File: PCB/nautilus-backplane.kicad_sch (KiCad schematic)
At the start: 85 parts

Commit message: Traced ethernet
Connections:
- removed net 0+: JP22.2 (B), JP40.3 (B), JP8.2 (B)
- removed net 0-: JP21.2 (B), JP40.2 (C), JP7.2 (B)
- net 0A+ renamed e2_0+
- net 0A- renamed e2_0-
- net 1+ renamed e1_1+
- net e1_1+: no longer JP20.2 (B)
- net 1- renamed e1_1-
- net e1_1-: no longer JP19.2 (B)
- net 1A+ renamed B12
- net B12: no longer JP24.2 (B)
- net 1A- renamed B13
- net B13: no longer JP23.2 (B)
- net 2+ renamed A19
- net A19: no longer JP4.2 (B)
- net 2- renamed A18
- net A18: no longer JP3.2 (B)
- net 3+ renamed A16
- net A16: no longer JP2.2 (B)
- net 3- renamed A17
- net A17: no longer JP1.2 (B)
- new net B18: JP40.2 (C)
- new net B19: JP40.3 (B)
- new net e1_0+: JP8.2 (B)
- new net e1_0-: JP7.2 (B)
- new net e1_2+: JP4.2 (B)
- new net e1_2-: JP3.2 (B)
- new net e1_3+: JP2.2 (B)
- new net e1_3-: JP1.2 (B)
- new net e2_1+: JP24.2 (B)
- new net e2_1-: JP23.2 (B)
- new net e2_2+: JP22.2 (B)
- new net e2_2-: JP21.2 (B)
- new net e2_3+: JP20.2 (B)
- new net e2_3-: JP19.2 (B)

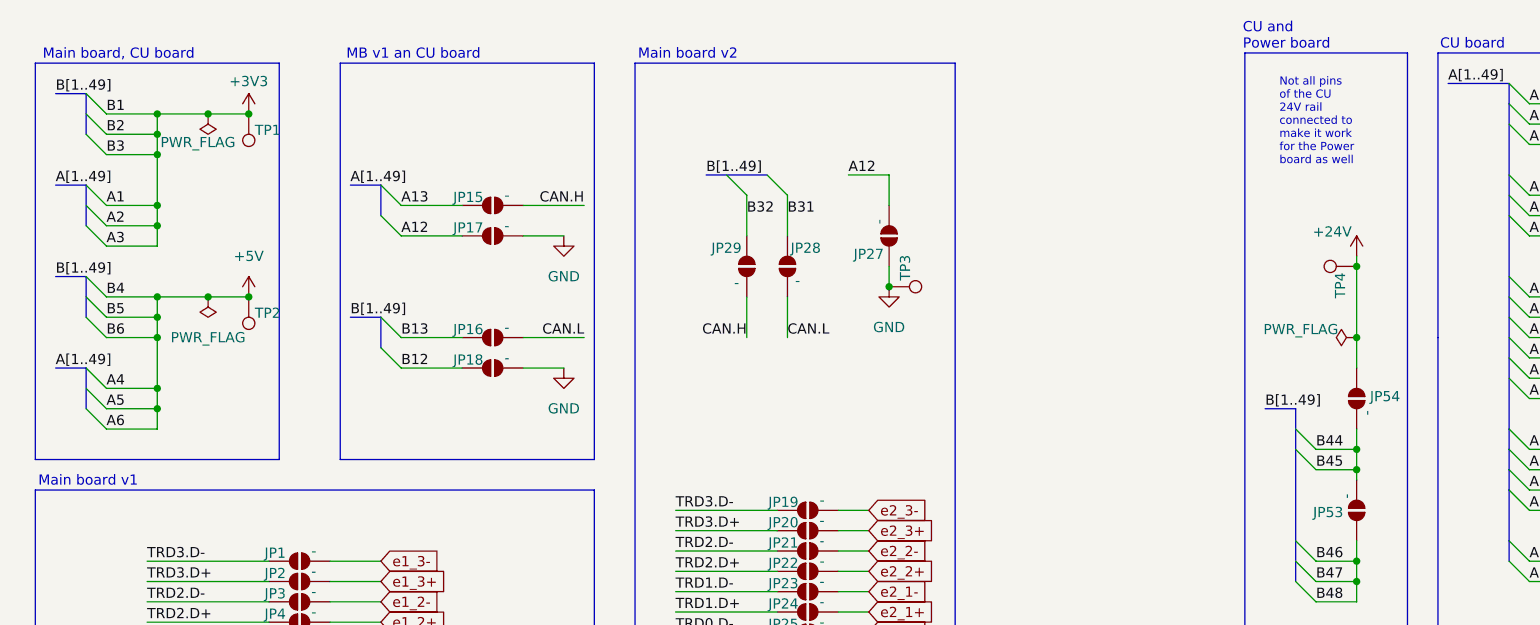
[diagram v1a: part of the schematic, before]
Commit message: placed banana connectors for power
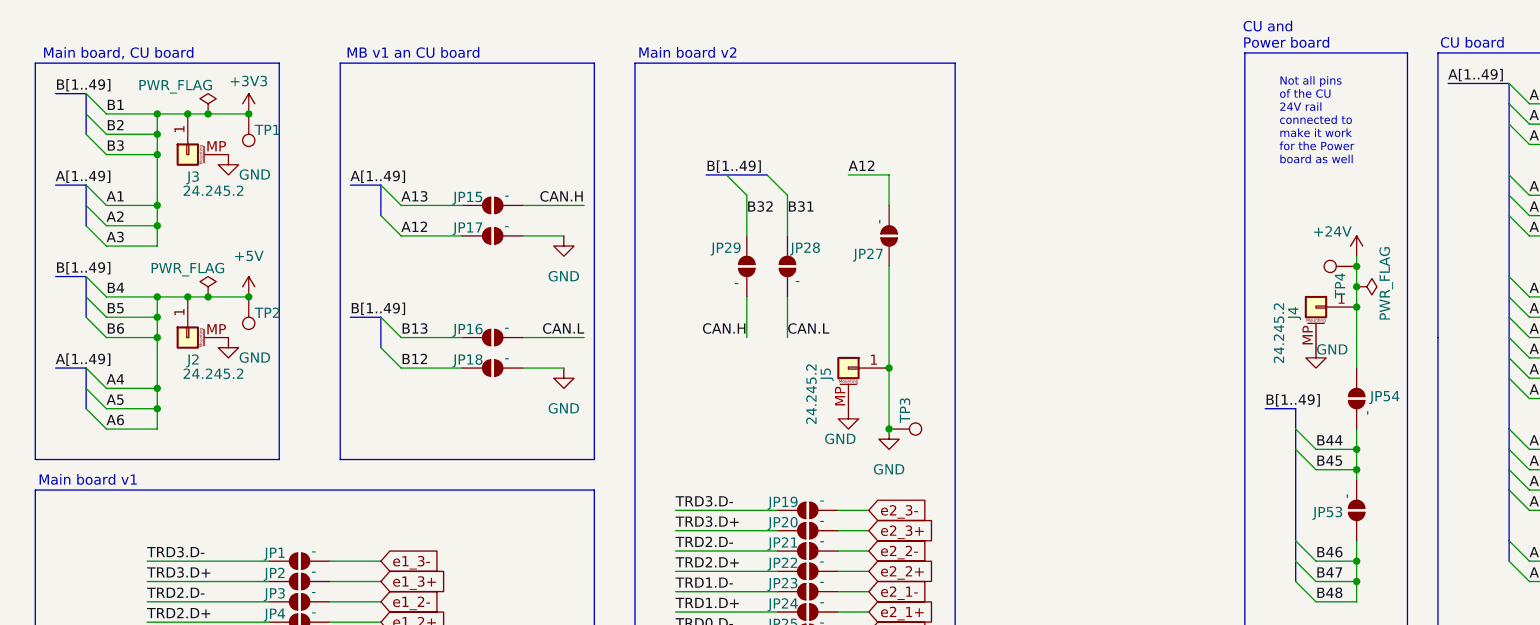
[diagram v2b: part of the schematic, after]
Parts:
- added J2, J3, J4, J5: 24.245.2, dz_con:ANT-TH_L33.0-W12.0, symbol #dzdb:s_con/CON-AMASS-24.245.2
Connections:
- net +24V: now also J4.1 (Pin_1)
- net +3V3: now also J3.1 (Pin_1)
- net +5V: now also J2.1 (Pin_1)
- net GND: now also J2.MP (MountPin), J3.MP (MountPin), J4.MP (MountPin), J5.1 (Pin_1), J5.MP (MountPin)
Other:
- moved on the sheet: TP3

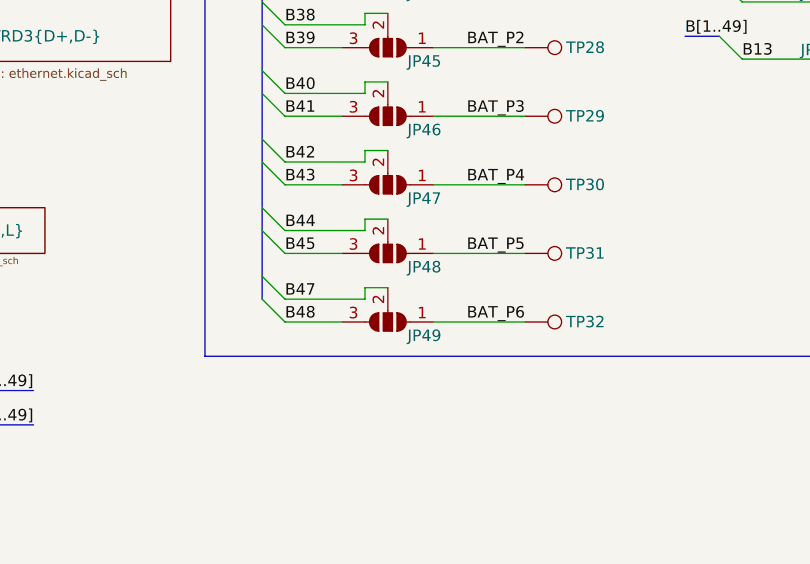
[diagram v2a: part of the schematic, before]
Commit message: Traced everything; TODO: tune trace length, fix drc error
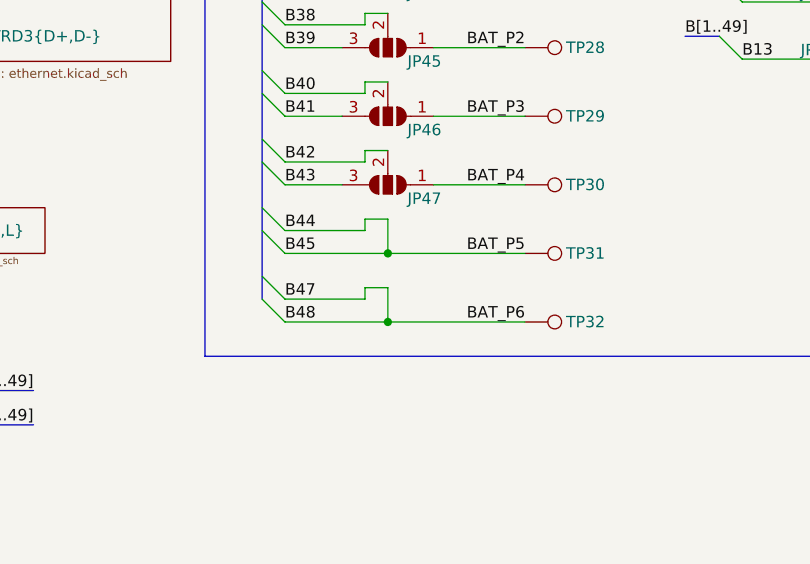
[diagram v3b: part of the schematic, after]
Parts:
- removed JP48, JP49: SolderJumper_3_Open, Jumper:SolderJumper-3_P1.3mm_Open_RoundedPad1.0x1.5mm, symbol Jumper:SolderJumper_3_Open
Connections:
- net BAT_P5 is gone; now on net B44: TP31.1
- net BAT_P6 is gone; now on net B46: TP32.1
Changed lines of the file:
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@@
 	)
 	(junction
+		(at 203.2 161.29)
+		(diameter 0)
+		(color 0 0 0 0)
+	)
+	(junction
 		(at 41.91 55.88)
 		(diameter 0)
@@
 		(color 0 0 0 0)
 	)
+	(junction
+		(at 203.2 153.67)
+		(diameter 0)
+		(color 0 0 0 0)
+	)
 	(bus_entry
 		(at 140.97 129.54)
@@
 	(wire
 		(pts
-			(xy 208.28 161.29) (xy 218.44 161.29)
-		)
-		(stroke
-			(width 0)
-			(type default)
-		)
-	)
-	(wire
-		(pts
 			(xy 191.77 54.61) (xy 191.77 62.23)
 		)
@@
 	(wire
 		(pts
+			(xy 203.2 161.29) (xy 218.44 161.29)
+		)
+		(stroke
+			(width 0)
+			(type default)
+		)
+	)
+	(wire
+		(pts
 			(xy 40.64 93.98) (xy 55.88 93.98)
 		)
@@
 	(wire
 		(pts
+			(xy 203.2 149.86) (xy 203.2 153.67)
+		)
+		(stroke
+			(width 0)
+			(type default)
+		)
+	)
+	(wire
+		(pts
 			(xy 73.66 148.59) (xy 68.58 148.59)
 		)
@@
 	(wire
 		(pts
-			(xy 191.77 161.29) (xy 198.12 161.29)
+			(xy 191.77 161.29) (xy 203.2 161.29)
 		)
 		(stroke
@@
 	(wire
 		(pts
+			(xy 203.2 157.48) (xy 203.2 161.29)
+		)
+		(stroke
+			(width 0)
+			(type default)
+		)
+	)
+	(wire
+		(pts
 			(xy 213.36 66.04) (xy 232.41 66.04)
 		)
@@
 	(wire
 		(pts
-			(xy 191.77 153.67) (xy 198.12 153.67)
+			(xy 191.77 153.67) (xy 203.2 153.67)
 		)
 		(stroke
@@
 	(wire
 		(pts
+			(xy 203.2 153.67) (xy 218.44 153.67)
+		)
+		(stroke
+			(width 0)
+			(type default)
+		)
+	)
+	(wire
+		(pts
 			(xy 44.45 177.8) (xy 44.45 176.53)
 		)
@@
 		)
 	)
-	(wire
-		(pts
-			(xy 208.28 153.67) (xy 218.44 153.67)
-		)
-		(stroke
-			(width 0)
-			(type default)
-		)
-	)
 	(label "CAN.L"
 		(at 120.65 58.42 0)
@@
 	(symbol
 		(lib_id "Jumper:SolderJumper_3_Open")
-		(at 203.2 161.29 180)
-		(unit 1)
-		(body_style 1)
-		(exclude_from_sim no)
-		(in_bom no)
-		(on_board yes)
-		(in_pos_files yes)
-		(dnp no)
-		(property "Reference" "JP49"
-			(at 207.264 162.814 0)
-			(show_name no)
-			(do_not_autoplace no)
-			(effects
-				(font
-					(size 1.27 1.27)
-				)
-			)
-		)
-		(property "Value" "SolderJumper_3_Open"
-			(at 203.2 165.1 0)
-			(hide yes)
-			(show_name no)
-			(do_not_autoplace no)
-			(effects
-				(font
-					(size 1.27 1.27)
-				)
-			)
-		)
-		(property "Footprint" "Jumper:SolderJumper-3_P1.3mm_Open_RoundedPad1.0x1.5mm"
-			(at 203.2 161.29 0)
-			(hide yes)
-			(show_name no)
-			(do_not_autoplace no)
-			(effects
-				(font
-					(size 1.27 1.27)
-				)
-			)
-		)
-		(property "Datasheet" ""
-			(at 203.2 146.05 0)
-			(hide yes)
-			(show_name no)
-			(do_not_autoplace no)
-			(effects
-				(font
-					(size 1.27 1.27)
-				)
-			)
-		)
-		(property "Description" "Solder Jumper, 3-pole, open"
-			(at 203.2 148.59 0)
-			(hide yes)
-			(show_name no)
-			(do_not_autoplace no)
-			(effects
-				(font
-					(size 1.27 1.27)
-				)
-			)
-		)
-		(property private "KLC_S5.1" "This is a generic symbol, it has fp-filter, but no default footprint"
-			(at 203.2 143.51 0)
-			(hide yes)
-			(show_name yes)
-			(do_not_autoplace no)
-			(effects
-				(font
-					(size 1.27 1.27)
-				)
-			)
-		)
-		(property private "KLC_S3.3" "Graphical-Symbol: thickness is 6mm, fill is background"
-			(at 203.2 140.97 0)
-			(hide yes)
-			(show_name yes)
-			(do_not_autoplace no)
-			(effects
-				(font
-					(size 1.27 1.27)
-				)
-			)
-		)
-		(pin "1"
-		)
-		(pin "3"
-		)
-		(pin "2"
-		)
-		(instances
-			(project "nautilus-backplane"
-				(path "/e08d3e09-d805-4650-baae-a4ad395cf0c7"
-					(reference "JP49")
-					(unit 1)
-				)
-			)
-		)
-	)
-	(symbol
-		(lib_id "Jumper:SolderJumper_3_Open")
 		(at 45.72 143.51 180)
 		(unit 1)
@@
 					(unit 1)
 				)
-			)
-		)
-	)
-	(symbol
-		(lib_id "Jumper:SolderJumper_3_Open")
-		(at 203.2 153.67 180)
-		(unit 1)
-		(body_style 1)
-		(exclude_from_sim no)
-		(in_bom no)
-		(on_board yes)
-		(in_pos_files yes)
-		(dnp no)
-		(property "Reference" "JP48"
-			(at 207.264 155.194 0)
-			(show_name no)
-			(do_not_autoplace no)
-			(effects
-				(font
-					(size 1.27 1.27)
-				)
-			)
-		)
-		(property "Value" "SolderJumper_3_Open"
-			(at 203.2 157.48 0)
-			(hide yes)
-			(show_name no)
-			(do_not_autoplace no)
-			(effects
-				(font
-					(size 1.27 1.27)
-				)
-			)
-		)
-		(property "Footprint" "Jumper:SolderJumper-3_P1.3mm_Open_RoundedPad1.0x1.5mm"
-			(at 203.2 153.67 0)
-			(hide yes)
-			(show_name no)
-			(do_not_autoplace no)
-			(effects
-				(font
-					(size 1.27 1.27)
-				)
-			)
-		)
-		(property "Datasheet" ""
-			(at 203.2 138.43 0)
-			(hide yes)
-			(show_name no)
-			(do_not_autoplace no)
-			(effects
-				(font
-					(size 1.27 1.27)
-				)
-			)
-		)
-		(property "Description" "Solder Jumper, 3-pole, open"
-			(at 203.2 140.97 0)
-			(hide yes)
-			(show_name no)
-			(do_not_autoplace no)
-			(effects
-				(font
-					(size 1.27 1.27)
-				)
-			)
-		)
-		(property private "KLC_S5.1" "This is a generic symbol, it has fp-filter, but no default footprint"
-			(at 203.2 135.89 0)
-			(hide yes)
-			(show_name yes)
-			(do_not_autoplace no)
-			(effects
-				(font
-					(size 1.27 1.27)
-				)
-			)
-		)
-		(property private "KLC_S3.3" "Graphical-Symbol: thickness is 6mm, fill is background"
-			(at 203.2 133.35 0)
-			(hide yes)
-			(show_name yes)
-			(do_not_autoplace no)
-			(effects
-				(font
-					(size 1.27 1.27)
-				)
-			)
-		)
-		(pin "1"
-		)
-		(pin "3"
-		)
-		(pin "2"
-		)
-		(instances
-			(project "nautilus-backplane"
-				(path "/e08d3e09-d805-4650-baae-a4ad395cf0c7"
-					(reference "JP48")
-					(unit 1)
-				)
